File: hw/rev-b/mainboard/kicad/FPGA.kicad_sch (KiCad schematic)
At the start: 46 parts, among them J17 PMOD1, J18 PMOD2, J22 PROG, J4 BUS_EXPANSION, J9 FPGA_MCU, Q1 MMBT3904, SW3 CONFIG, U10 T20Q144C3

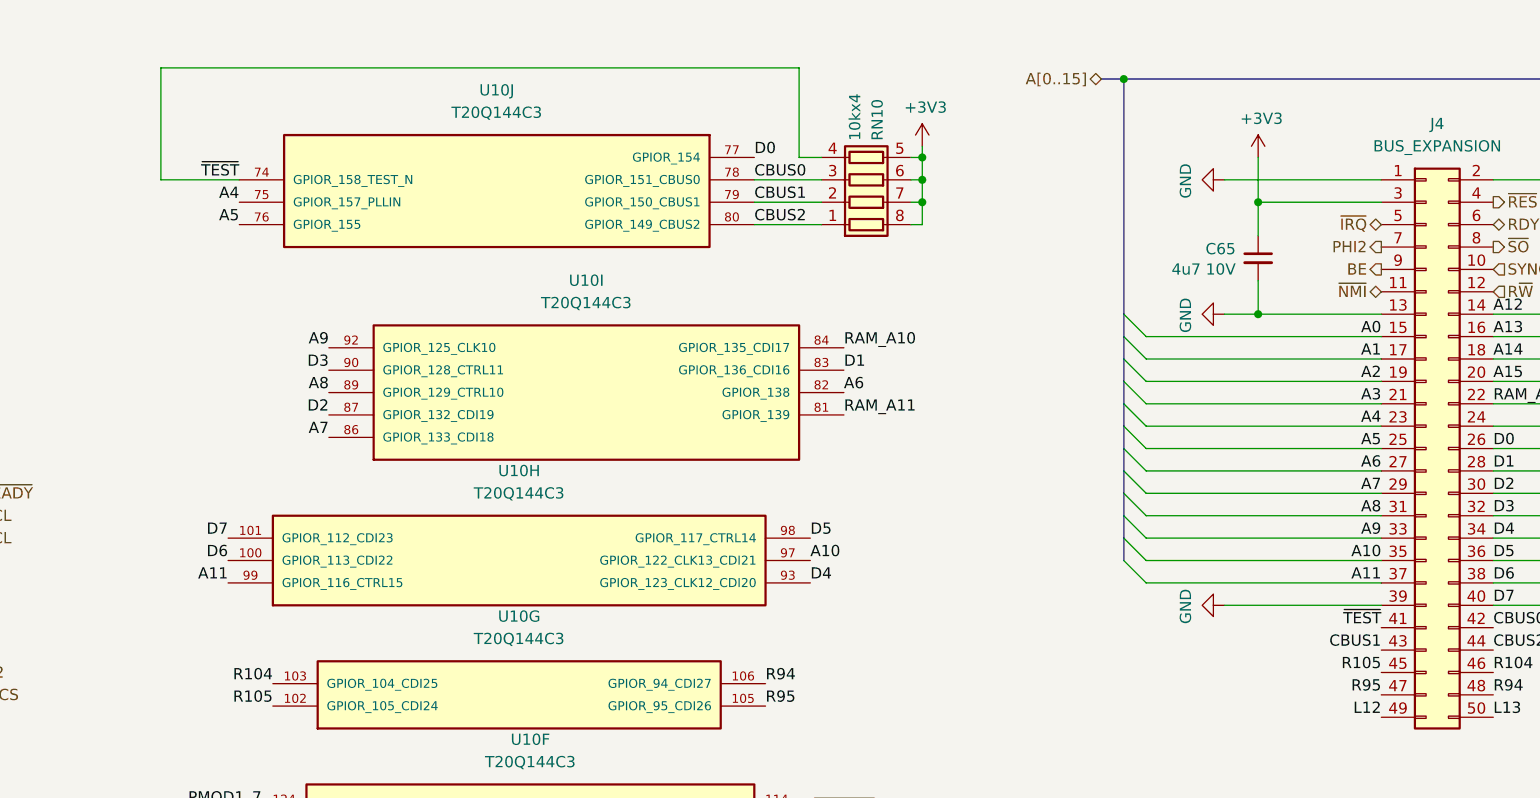
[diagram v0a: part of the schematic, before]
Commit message: hw: repurpose SP0 (spare) for independent VSYNC
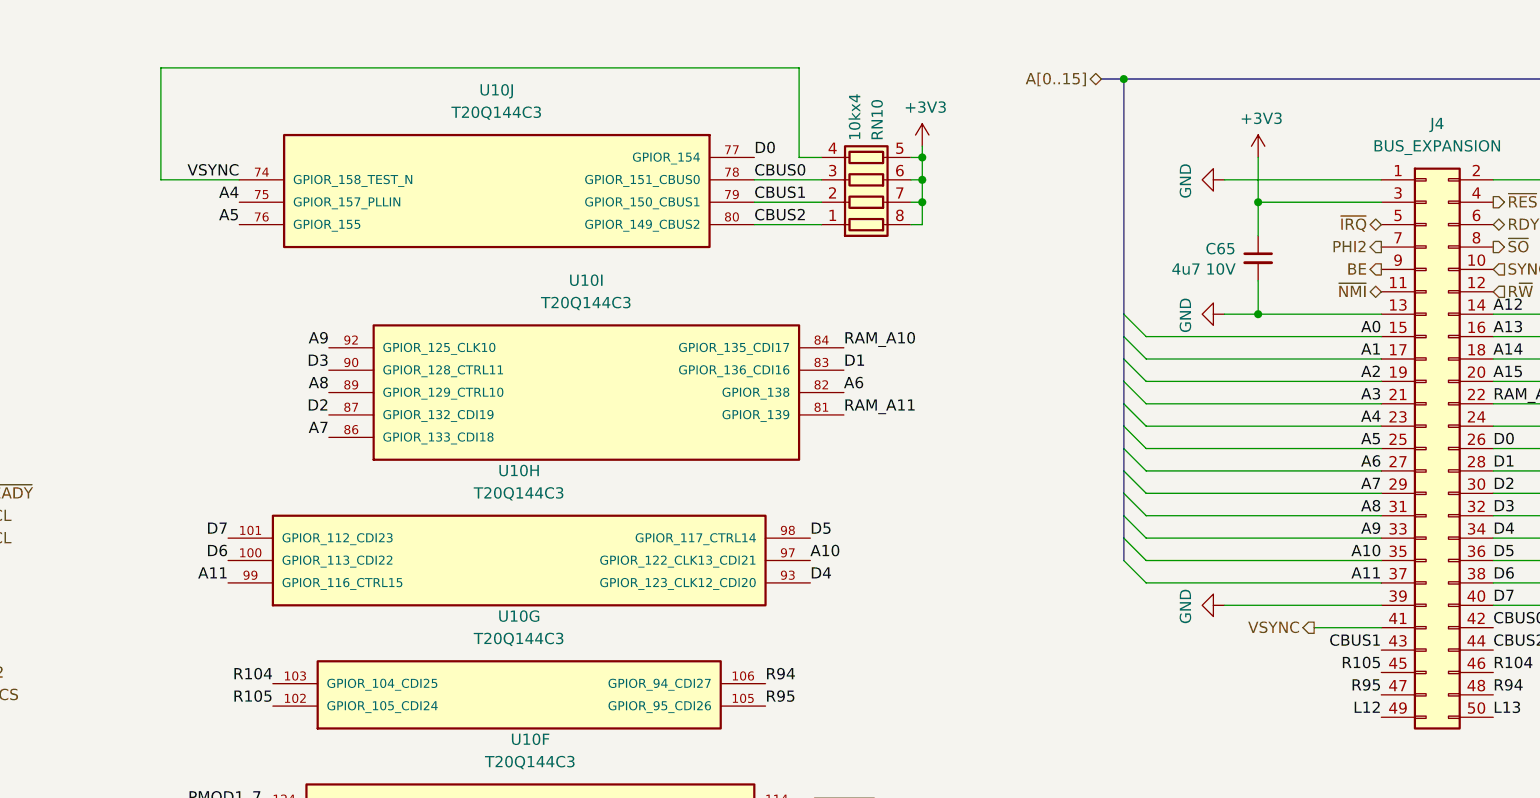
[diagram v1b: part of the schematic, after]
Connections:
- net ~{TEST} renamed VSYNC
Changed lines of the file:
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@@
 	(wire
 		(pts
+			(xy 368.3 137.16) (xy 375.92 137.16)
+		)
+		(stroke
+			(width 0)
+			(type default)
+		)
+	)
+	(wire
+		(pts
 			(xy 299.72 43.18) (xy 312.42 43.18)
 		)
@@
 		)
 	)
-	(label "~{TEST}"
-		(at 375.92 137.16 180)
-		(fields_autoplaced yes)
-		(effects
-			(font
-				(size 1.27 1.27)
-			)
-			(justify right bottom)
-		)
-	)
 	(label "SPI0_TX"
 		(at 204.47 50.8 180)
@@
 		)
 	)
-	(label "~{TEST}"
+	(label "VSYNC"
 		(at 246.38 86.36 180)
 		(fields_autoplaced yes)
@@
 		)
 	)
+	(hierarchical_label "VSYNC"
+		(shape output)
+		(at 368.3 137.16 180)
+		(fields_autoplaced yes)
+		(effects
+			(font
+				(size 1.27 1.27)
+			)
+			(justify right)
+		)
+	)

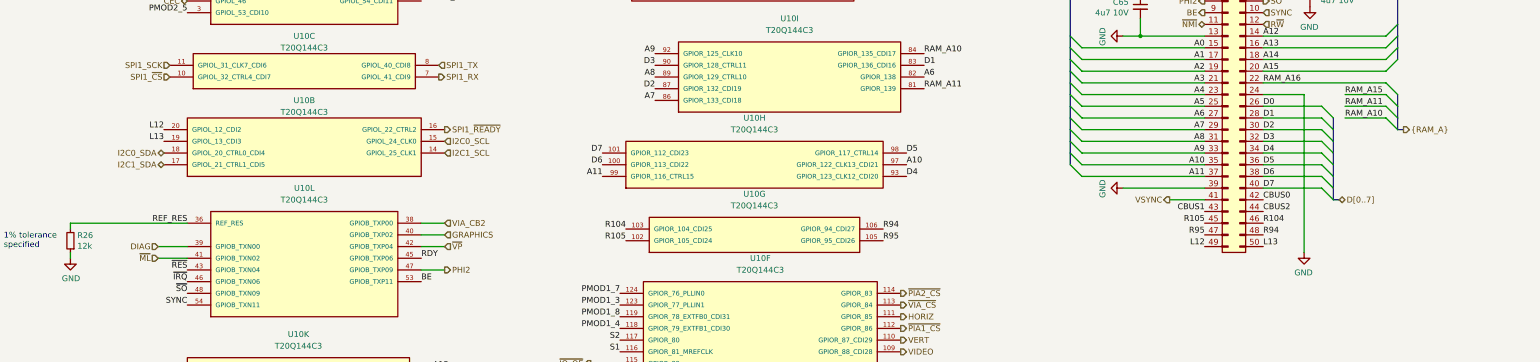
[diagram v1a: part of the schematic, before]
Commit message: hw: audio_det, stitching around sram
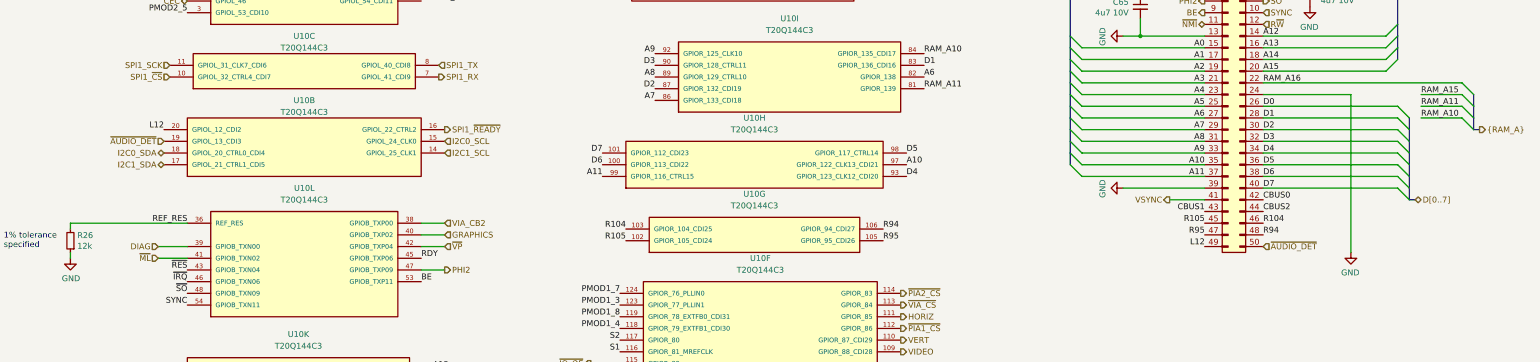
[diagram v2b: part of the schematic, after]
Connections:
- net L13 renamed ~{AUDIO_DET}
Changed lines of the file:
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@@
 	)
 	(bus_entry
-		(at 417.83 114.3)
+		(at 434.34 114.3)
 		(size -2.54 -2.54)
 		(stroke
@@
 	)
 	(bus_entry
-		(at 403.86 124.46)
+		(at 420.37 124.46)
 		(size -2.54 -2.54)
 		(stroke
@@
 	)
 	(bus_entry
-		(at 417.83 119.38)
+		(at 434.34 119.38)
 		(size -2.54 -2.54)
 		(stroke
@@
 	)
 	(bus_entry
-		(at 417.83 121.92)
+		(at 434.34 121.92)
 		(size -2.54 -2.54)
 		(stroke
@@
 	)
 	(bus_entry
-		(at 403.86 121.92)
+		(at 420.37 121.92)
 		(size -2.54 -2.54)
 		(stroke
@@
 	)
 	(bus_entry
-		(at 403.86 119.38)
+		(at 420.37 119.38)
 		(size -2.54 -2.54)
 		(stroke
@@
 	)
 	(bus_entry
-		(at 403.86 127)
+		(at 420.37 127)
 		(size -2.54 -2.54)
 		(stroke
@@
 	)
 	(bus_entry
-		(at 417.83 116.84)
+		(at 434.34 116.84)
 		(size -2.54 -2.54)
 		(stroke
@@
 	)
 	(bus_entry
-		(at 403.86 132.08)
+		(at 420.37 132.08)
 		(size -2.54 -2.54)
 		(stroke
@@
 	)
 	(bus_entry
-		(at 403.86 134.62)
+		(at 420.37 134.62)
 		(size -2.54 -2.54)
 		(stroke
@@
 	)
 	(bus_entry
-		(at 403.86 137.16)
+		(at 420.37 137.16)
 		(size -2.54 -2.54)
 		(stroke
@@
 	)
 	(bus_entry
-		(at 403.86 129.54)
+		(at 420.37 129.54)
 		(size -2.54 -2.54)
 		(stroke
@@
 	(bus
 		(pts
-			(xy 403.86 137.16) (xy 405.13 137.16)
+			(xy 420.37 137.16) (xy 421.64 137.16)
 		)
 		(stroke
@@
 	(wire
 		(pts
-			(xy 388.62 119.38) (xy 401.32 119.38)
+			(xy 388.62 119.38) (xy 417.83 119.38)
 		)
 		(stroke
@@
 	(bus
 		(pts
-			(xy 403.86 132.08) (xy 403.86 134.62)
+			(xy 420.37 132.08) (xy 420.37 134.62)
 		)
 		(stroke
@@
 	(bus
 		(pts
-			(xy 417.83 119.38) (xy 417.83 121.92)
+			(xy 434.34 119.38) (xy 434.34 121.92)
 		)
 		(stroke
@@
 	(bus
 		(pts
-			(xy 403.86 121.92) (xy 403.86 124.46)
+			(xy 420.37 121.92) (xy 420.37 124.46)
 		)
 		(stroke
@@
 	(bus
 		(pts
-			(xy 403.86 134.62) (xy 403.86 137.16)
+			(xy 420.37 134.62) (xy 420.37 137.16)
 		)
 		(stroke
@@
 	(wire
 		(pts
-			(xy 388.62 129.54) (xy 401.32 129.54)
+			(xy 388.62 129.54) (xy 417.83 129.54)
 		)
 		(stroke
@@
 	(bus
 		(pts
-			(xy 403.86 129.54) (xy 403.86 132.08)
+			(xy 420.37 129.54) (xy 420.37 132.08)
 		)
 		(stroke
@@
 	(wire
 		(pts
-			(xy 388.62 127) (xy 401.32 127)
+			(xy 388.62 127) (xy 417.83 127)
 		)
 		(stroke
@@
 	(wire
 		(pts
-			(xy 406.4 114.3) (xy 415.29 114.3)
+			(xy 422.91 114.3) (xy 431.8 114.3)
 		)
 		(stroke
@@
 	(bus
 		(pts
-			(xy 403.86 119.38) (xy 403.86 121.92)
+			(xy 420.37 119.38) (xy 420.37 121.92)
 		)
 		(stroke
@@
 	(wire
 		(pts
-			(xy 397.51 114.3) (xy 388.62 114.3)
+			(xy 407.67 114.3) (xy 388.62 114.3)
 		)
 		(stroke
@@
 	(bus
 		(pts
-			(xy 417.83 114.3) (xy 417.83 116.84)
+			(xy 434.34 114.3) (xy 434.34 116.84)
 		)
 		(stroke
@@
 	(wire
 		(pts
-			(xy 388.62 132.08) (xy 401.32 132.08)
+			(xy 388.62 132.08) (xy 417.83 132.08)
 		)
 		(stroke
@@
 	(wire
 		(pts
-			(xy 388.62 121.92) (xy 401.32 121.92)
+			(xy 388.62 121.92) (xy 417.83 121.92)
 		)
 		(stroke
@@
 	(bus
 		(pts
-			(xy 417.83 116.84) (xy 417.83 119.38)
+			(xy 434.34 116.84) (xy 434.34 119.38)
 		)
 		(stroke
@@
 	(bus
 		(pts
-			(xy 417.83 121.92) (xy 419.1 121.92)
+			(xy 434.34 121.92) (xy 435.61 121.92)
 		)
 		(stroke
@@
 	(wire
 		(pts
-			(xy 388.62 124.46) (xy 401.32 124.46)
+			(xy 388.62 124.46) (xy 417.83 124.46)
 		)
 		(stroke
@@
 	(wire
 		(pts
-			(xy 406.4 119.38) (xy 415.29 119.38)
+			(xy 422.91 119.38) (xy 431.8 119.38)
 		)
 		(stroke
@@
 	(wire
 		(pts
-			(xy 388.62 134.62) (xy 401.32 134.62)
+			(xy 388.62 134.62) (xy 417.83 134.62)
 		)
 		(stroke
@@
 	(wire
 		(pts
-			(xy 406.4 116.84) (xy 415.29 116.84)
+			(xy 422.91 116.84) (xy 431.8 116.84)
 		)
 		(stroke
@@
 	(wire
 		(pts
-			(xy 388.62 116.84) (xy 401.32 116.84)
+			(xy 388.62 116.84) (xy 417.83 116.84)
 		)
 		(stroke
@@
 	(wire
 		(pts
-			(xy 397.51 148.59) (xy 397.51 114.3)
+			(xy 407.67 148.59) (xy 407.67 114.3)
 		)
 		(stroke
@@
 	(bus
 		(pts
-			(xy 403.86 124.46) (xy 403.86 127)
+			(xy 420.37 124.46) (xy 420.37 127)
 		)
 		(stroke
@@
 	(wire
 		(pts
-			(xy 388.62 111.76) (xy 415.29 111.76)
+			(xy 388.62 111.76) (xy 431.8 111.76)
 		)
 		(stroke
@@
 	(bus
 		(pts
-			(xy 403.86 127) (xy 403.86 129.54)
+			(xy 420.37 127) (xy 420.37 129.54)
 		)
 		(stroke
@@
 	)
 	(label "RAM_A10"
-		(at 406.4 119.38 0)
+		(at 422.91 119.38 0)
 		(fields_autoplaced yes)
 		(effects
@@
 		)
 	)
-	(label "L13"
-		(at 149.86 124.46 180)
-		(fields_autoplaced yes)
-		(effects
-			(font
-				(size 1.27 1.27)
-			)
-			(justify right bottom)
-		)
-	)
 	(label "CDONE"
 		(at 128.27 41.91 0)
@@
 	)
 	(label "RAM_A15"
-		(at 406.4 114.3 0)
+		(at 422.91 114.3 0)
 		(fields_autoplaced yes)
 		(effects
@@
 		)
 	)
-	(label "L13"
-		(at 388.62 147.32 0)
-		(fields_autoplaced yes)
-		(effects
-			(font
-				(size 1.27 1.27)
-			)
-			(justify left bottom)
-		)
-	)
 	(label "TDI"
 		(at 130.81 57.15 0)
@@
 	)
 	(label "RAM_A11"
-		(at 406.4 116.84 0)
+		(at 422.91 116.84 0)
 		(fields_autoplaced yes)
 		(effects
@@
 	(hierarchical_label "{RAM_A}"
 		(shape output)
-		(at 419.1 121.92 0)
+		(at 435.61 121.92 0)
 		(fields_autoplaced yes)
 		(effects
@@
 		)
 	)
+	(hierarchical_label "~{AUDIO_DET}"
+		(shape input)
+		(at 149.86 124.46 180)
+		(fields_autoplaced yes)
+		(effects
+			(font
+				(size 1.27 1.27)
+			)
+			(justify right)
+		)
+	)
 	(hierarchical_label "~{IO_OE}"
 		(shape output)
@@
 	(hierarchical_label "D[0..7]"
 		(shape bidirectional)
-		(at 405.13 137.16 0)
+		(at 421.64 137.16 0)
 		(fields_autoplaced yes)
 		(effects
@@
 		)
 	)
+	(hierarchical_label "~{AUDIO_DET}"
+		(shape input)
+		(at 388.62 147.32 0)
+		(fields_autoplaced yes)
+		(effects
+			(font
+				(size 1.27 1.27)
+			)
+			(justify left)
+		)
+	)
 	(hierarchical_label "SPI1_~{READY}"
 		(shape output)
@@
 	(symbol
 		(lib_id "power:GND")
-		(at 397.51 148.59 0)
+		(at 407.67 148.59 0)
 		(mirror y)
 		(unit 1)
@@
 		(dnp no)
 		(property "Reference" "#PWR085"
-			(at 397.51 154.94 0)
+			(at 407.67 154.94 0)
 			(effects
 				(font
@@
 		)
 		(property "Value" "GND"
-			(at 397.383 152.9842 0)
+			(at 407.543 152.9842 0)
 			(effects
 				(font
@@
 		)
 		(property "Footprint" ""
-			(at 397.51 148.59 0)
+			(at 407.67 148.59 0)
 			(effects
 				(font
@@
 		)
 		(property "Datasheet" ""
-			(at 397.51 148.59 0)
+			(at 407.67 148.59 0)
 			(effects
 				(font
@@
 		)
 		(property "Description" "Power symbol creates a global label with name \"GND\" , ground"
-			(at 397.51 148.59 0)
+			(at 407.67 148.59 0)
 			(effects
 				(font
